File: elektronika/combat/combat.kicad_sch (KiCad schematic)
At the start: 4 parts, among them J1 Conn_01x04_Pin, U1 ESP32-S3-WROOM, U2 TB6612FNG, U3 L78M05CDT

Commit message: schemat pcb prawie gotowy
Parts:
- removed U3: L78M05CDT, VREG_L78M05CDT, symbol L78M05CDT:L78M05CDT
- added C1: 10uF, symbol Device:C
- added C2: 22uF, symbol Device:C
- added D1: D_Schottky, Diode_THT:D_DO-41_SOD81_P10.16mm_Horizontal, symbol Device:D_Schottky
- added J2: naped_prawy, TerminalBlock:TerminalBlock_MaiXu_MX126-5.0-02P_1x02_P5.00mm, symbol Connector:Screw_Terminal_01x02
- added J3: naped_lewy, TerminalBlock:TerminalBlock_MaiXu_MX126-5.0-02P_1x02_P5.00mm, symbol Connector:Screw_Terminal_01x02
- added R1: 240, PCM_SparkFun-Resistor:R_0603_1608Metric, symbol PCM_SparkFun-Resistor:R
- added R2: 390, PCM_SparkFun-Resistor:R_0603_1608Metric, symbol PCM_SparkFun-Resistor:R
- added U3: AMS1117, Package_TO_SOT_SMD:SOT-223-3_TabPin2, symbol Regulator_Linear:AMS1117
- added U4: przetwornica, Connector_PinHeader_1.00mm:Bez_nazwy, symbol chuj_wie:przetwornica_pot
- J1: footprint (none) -> Connector_PinHeader_2.54mm:PinHeader_1x04_P2.54mm_Vertical
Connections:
- net GND: now reaches U2.10 (PGND2), U2.9 (PGND2)
- net GND: now also J1.4 (Pin_4), U1.1 (GND), U1.40 (GND), U1.41.1 (GND), U1.41.2 (GND), U1.41.3 (GND), U1.41.4 (GND), U1.41.5 (GND), U1.41.6 (GND), U1.41.7 (GND), U1.41.8 (GND), U1.41.9 (GND), U2.18 (GND), U2.3 (PGND1), U2.4 (PGND1), C1.2, C2.1, R2.2, U4. (IN+)
- net +3.3V: now reaches U2.19 (STBY)
- net +3.3V: now also U1.2 (VDD), C2.2, D1.2 (A), R1.1, U3.2 (VO)
- net +5V: now reaches U2.20 (VCC)
- net +5V: now also J1.3 (Pin_3), C1.1, D1.1 (K), U3.3 (VI), U4. (IN+)
- net RX: now reaches J1.1 (Pin_1)
- net RX: now also U1.10 (IOA17)
- net TX: now reaches J1.2 (Pin_2)
- net TX: now also U1.11 (IOA18)
- new net: R1.2, R2.1, U3.1 (ADJ)
- new net 11.1V: U4. (IN+)
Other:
- moved on the sheet: J1

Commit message: płytka pcb bez footprinta
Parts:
- removed U1: ESP32-S3-WROOM, PCM_SparkFun-RF:ESP32-S3-WROOM-1, symbol PCM_SparkFun-RF:ESP32-S3-WROOM
- removed U2: TB6612FNG, Package_SO:SSOP-24_5.3x8.2mm_P0.65mm, symbol Driver_Motor:TB6612FNG
- added C5: 1u, Capacitor_SMD:C_0603_1608Metric, symbol Device:C
- added D2: RED, LED_SMD:LED_0603_1608Metric, symbol Device:LED
- added D3: GREEN, LED_SMD:LED_0603_1608Metric, symbol Device:LED
- added D4: BLUE, LED_SMD:LED_0603_1608Metric, symbol Device:LED
- added J4: TYPE-C-31-M-12, TYPE-C-31-M-12:HRO_TYPE-C-31-M-12, symbol TYPE-C-31-M-12:TYPE-C-31-M-12
- added R3, R4, R5, R6, R7, R8: 5.1K, Resistor_SMD:R_0603_1608Metric, symbol Device:R
- added SW1, SW2: TS-1088-AR02016, easyeda2kicad:SW-SMD_L3.9-W3.0-P4.45, symbol easyeda2kicad:TS-1088-AR02016
- added TB1: POLOLU-713, foots:SHIELD_POLOLU-713, symbol POLOLU-713:POLOLU-713
- added U1: ESP32-S3-WROOM-1, Espressif:ESP32-S3-WROOM-1, symbol Espressif:ESP32-S3-WROOM-1
- R1: value 240 -> 390
- R2: value 390 -> 240
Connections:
- net +3.3V: now also U1.2 (3V3)
- net +5V: now also J4.A4_B9 (VBUS), J4.B4_A9 (VBUS), R5.1
- net GND: now also C5.2, D2.1 (K), D3.1 (K), D4.1 (K), J4.A1_B12 (GND), J4.B1_A12 (GND), J4.S1 (SHIELD), J4.S2 (SHIELD), J4.S3 (SHIELD), J4.S4 (SHIELD), R3.2, R4.2, SW1.1, SW2.1, TB1.1 (GND), TB1.8 (GND), TB1.9 (GND)
- net RX: now also U1.10 (GPIO17/U1TXD/ADC2_CH6)
- net TX: now also U1.11 (GPIO18/U1RXD/ADC2_CH7/CLK_OUT3)
- net B01: now reaches J2.1 (Pin_1)
- net B01: now also TB1.6 (BO1)
- net B02: now reaches J2.2 (Pin_2)
- net B02: now also TB1.5 (BO2)
- net A01: now reaches J3.1 (Pin_1)
- net A01: now also TB1.3 (AO1)
- net A02: now reaches J3.2 (Pin_2)
- net A02: now also TB1.4 (AO2)
- new net: D4.2 (A), R7.2
- new net: D2.2 (A), R5.2
- new net: J4.B5 (CC2), R4.1
- new net: D3.2 (A), R6.2
- new net: J4.A5 (CC1), R3.1
- new net: U1.1 (GND), U1.40 (GND), U1.41 (GND)
- new net +3V3: R6.1, R8.1
- new net 3V3: TB1.13 (~{STBY})
- new net D+: J4.A6 (DP1), J4.B6 (DP2), U1.14 (GPIO20/U1CTS/ADC2_CH9/CLK_OUT1/USB_D+)
- new net D-: J4.A7 (DN1), J4.B7 (DN2), U1.13 (GPIO19/U1RTS/ADC2_CH8/CLK_OUT2/USB_D-)
- new net EN: C5.1, R8.2, SW1.2, U1.3 (EN)
- new net GPIO0: SW2.2, U1.27 (GPIO0/BOOT)
- new net GPIO21: R7.1, U1.23 (GPIO21)
- no-connect marks 0 -> 2

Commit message: gotowy schemat pcb bez footow
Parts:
- added J5: Screw_Terminal_01x03, symbol Connector:Screw_Terminal_01x03
- added U2: (no value), symbol SterownikBLDC:BLDC_BlHeli
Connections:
- net 11.1V: now also TB1.7 (VMOT), U2. (GND)
- net 3V3: now also TB1.2 (VCC)
- net GND: now also U1.1 (GND), U1.40 (GND), U1.41 (GND), U2. (GND)
- net GPIO10: now reaches TB1.10 (PWMB)
- net GPIO10: now also U1.18 (GPIO10/TOUCH10/ADC1_CH9/FSPICS0/FSPIIO4/SUBSPICS0)
- net GPIO9: now reaches TB1.11 (BIN2)
- net GPIO9: now also U1.17 (GPIO9/TOUCH9/ADC1_CH8/FSPIHD/SUBSPIHD)
- net GPIO8: now reaches TB1.12 (BIN1)
- net GPIO8: now also U1.12 (GPIO8/TOUCH8/ADC1_CH7/SUBSPICS1)
- net GPIO5: now reaches TB1.14 (AIN1)
- net GPIO5: now also U1.5 (GPIO5/TOUCH5/ADC1_CH4)
- net GPIO6: now reaches TB1.15 (AIN2)
- net GPIO6: now also U1.6 (GPIO6/TOUCH6/ADC1_CH5)
- net GPIO7: now reaches TB1.16 (PWMA)
- net GPIO7: now also U1.7 (GPIO7/TOUCH7/ADC1_CH6)
- net ePWM: now reaches U1.4 (GPIO4/TOUCH4/ADC1_CH3)
- net ePWM: now also U2. (GND)
- new net: J5.1 (Pin_1), U2. (GND)
- new net: J5.2 (Pin_2), U2. (GND)
- new net: J5.3 (Pin_3), U2. (GND)
- no-connect marks 2 -> 25
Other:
- moved on the sheet: J4, R3, R4, TB1

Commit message: nowsza wersja schematu
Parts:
- added H1, H2, H3, H4: MountingHole, symbol Mechanical:MountingHole
- C1: footprint (none) -> Capacitor_SMD:C_0805_2012Metric_Pad1.18x1.45mm_HandSolder
- C2: footprint (none) -> Capacitor_SMD:C_1210_3225Metric_Pad1.33x2.70mm_HandSolder
- J4: footprint TYPE-C-31-M-12:HRO_TYPE-C-31-M-12 -> Connector_USB:USB_C_Receptacle_HRO_TYPE-C-31-M-12
- J5: footprint (none) -> PCM_SparkFun-Connector:ScrewTerminal_1x03_P3.5mm_Blue
- SW1, SW2: footprint easyeda2kicad:SW-SMD_L3.9-W3.0-P4.45 -> foots:PTS125SM73SMTR21MLFS
- U2: value (none) -> kontroler_bldc

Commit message: gotowy footprint
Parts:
- removed J4: TYPE-C-31-M-12, Connector_USB:USB_C_Receptacle_HRO_TYPE-C-31-M-12, symbol TYPE-C-31-M-12:TYPE-C-31-M-12
- removed R3, R4: 5.1K, Resistor_SMD:R_0603_1608Metric, symbol Device:R
- removed SW1, SW2: TS-1088-AR02016, foots:PTS125SM73SMTR21MLFS, symbol easyeda2kicad:TS-1088-AR02016
- added J4: USB_C_Receptacle_USB2.0_14P, Connector_USB:USB_C_Receptacle_HRO_TYPE-C-31-M-12, symbol Connector:USB_C_Receptacle_USB2.0_14P
- added J6: Conn_02x04_Odd_Even, Connector_PinHeader_2.54mm:PinHeader_2x04_P2.54mm_Vertical, symbol Connector_Generic:Conn_02x04_Odd_Even
- added J7: Conn_01x02, PCM_SparkFun-Connector:ScrewTerminal_1x02_P3.5mm_Blue, symbol Connector_Generic:Conn_01x02
- added R10, R11: 5.1K, Resistor_SMD:R_0603_1608Metric, symbol Device:R
- added SW1, SW3: SW_DIP_x01, foots:gownoklik, symbol Switch:SW_DIP_x01
- H1, H2, H3, H4: footprint (none) -> MountingHole:MountingHole_3.2mm_M3
- J2, J3: footprint TerminalBlock:TerminalBlock_MaiXu_MX126-5.0-02P_1x02_P5.00mm -> PCM_SparkFun-Connector:ScrewTerminal_1x02_P3.5mm_Blue
- R6, R7: value 5.1K -> 1k
- U2: footprint (none) -> foots:BLDC
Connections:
- net +5V: now also U4.3 (OUT+), J4.A4 (VBUS), J4.A9 (VBUS), J4.B4 (VBUS), J4.B9 (VBUS); no longer U4. (IN+)
- net 11.1V: now also U2.1 (+11.1V), U4.4 (IN+); no longer U2. (GND), U4. (IN+)
- net 3V3: now also J6.1 (Pin_1)
- net D+: now also J4.A6 (D+), J4.B6 (D+)
- net D-: now also J4.A7 (D-), J4.B7 (D-)
- net EN: now also SW1.2
- net GND: now also U2.3 (LGND), U2.4 (GND), U4.1 (OUT-), U4.2 (IN-), J4.A1 (GND), J4.A12 (GND), J4.B1 (GND), J4.B12 (GND), J4.SH (SHIELD), J6.8 (Pin_8), R10.2, R11.2, SW1.1, SW3.1; no longer U2. (GND), U4. (IN+)
- net GPIO0: now also SW3.2
- net RX: now also J6.2 (Pin_2)
- net TX: now also J6.7 (Pin_7)
- net ePWM: now also U2.2 (PWM); no longer U2. (GND)
- net at J5.1 (Pin_1): now also U2.7 (-); no longer U2. (GND)
- net at J5.2 (Pin_2): now also U2.6 (PWM); no longer U2. (GND)
- net at J5.3 (Pin_3): now also U2.5 (+); no longer U2. (GND)
- new net: J4.A5 (CC1), R10.1
- new net: J4.B5 (CC2), R11.1
- no-connect marks 25 -> 27
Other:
- moved on the sheet: C5, J1, R8

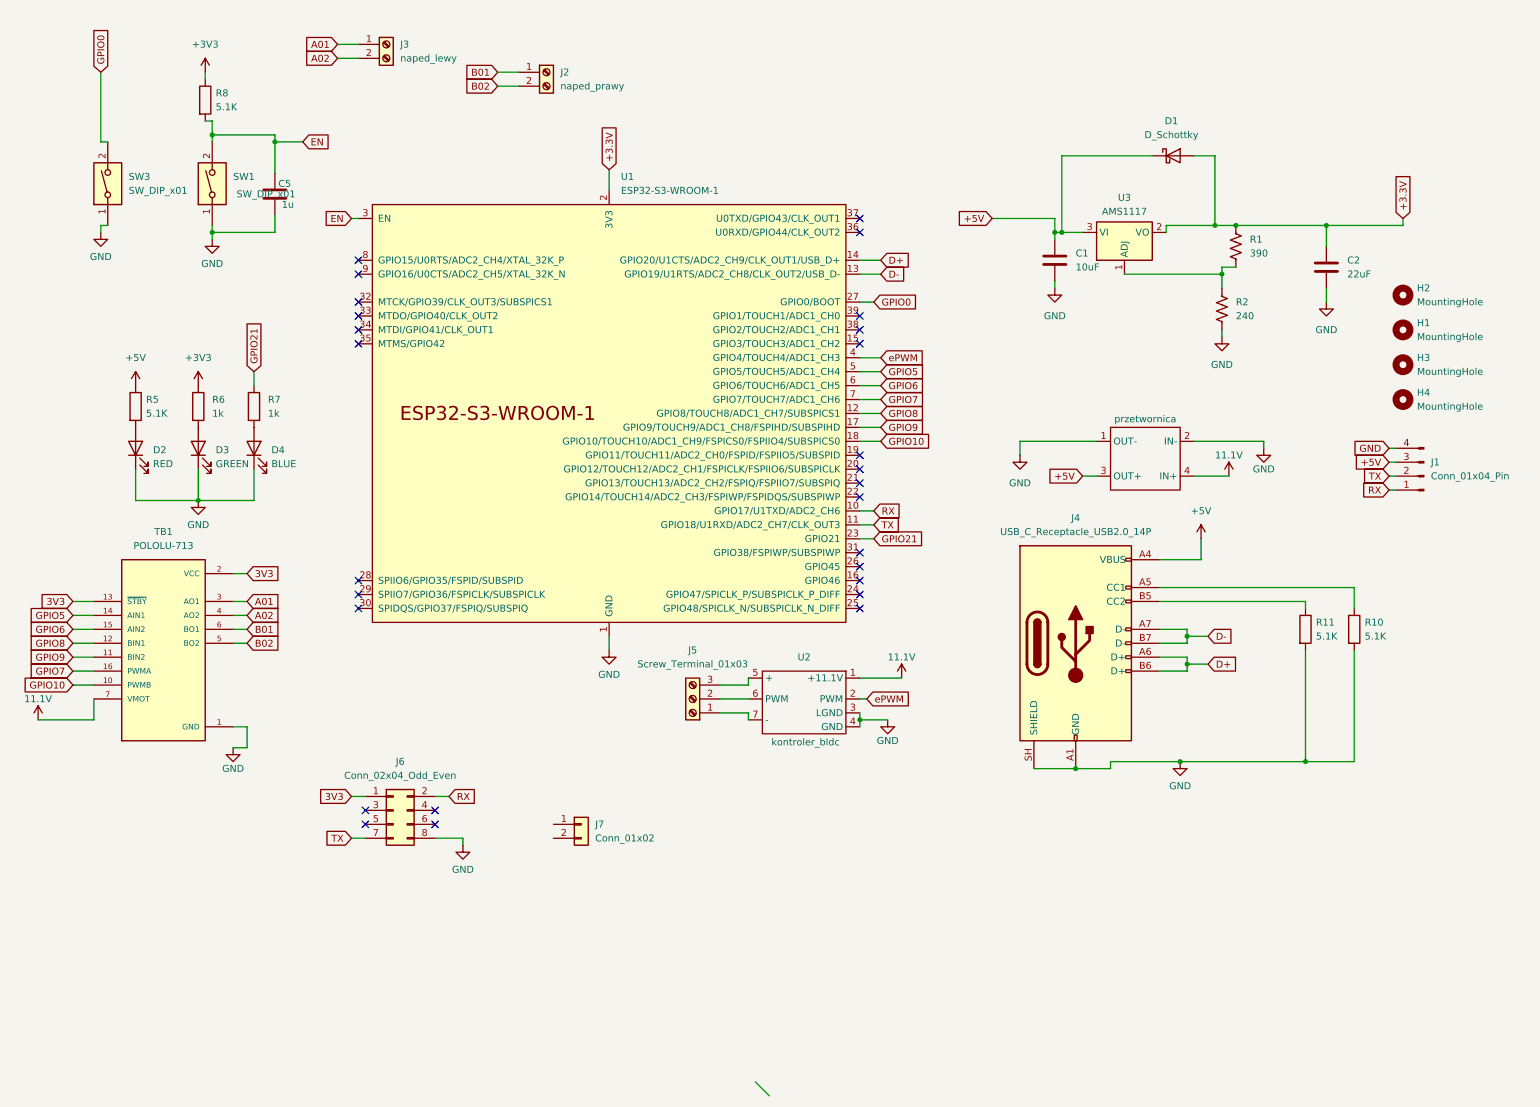
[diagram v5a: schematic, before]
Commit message: lepsza wersja pcb, layout jeszcze do zrobienia
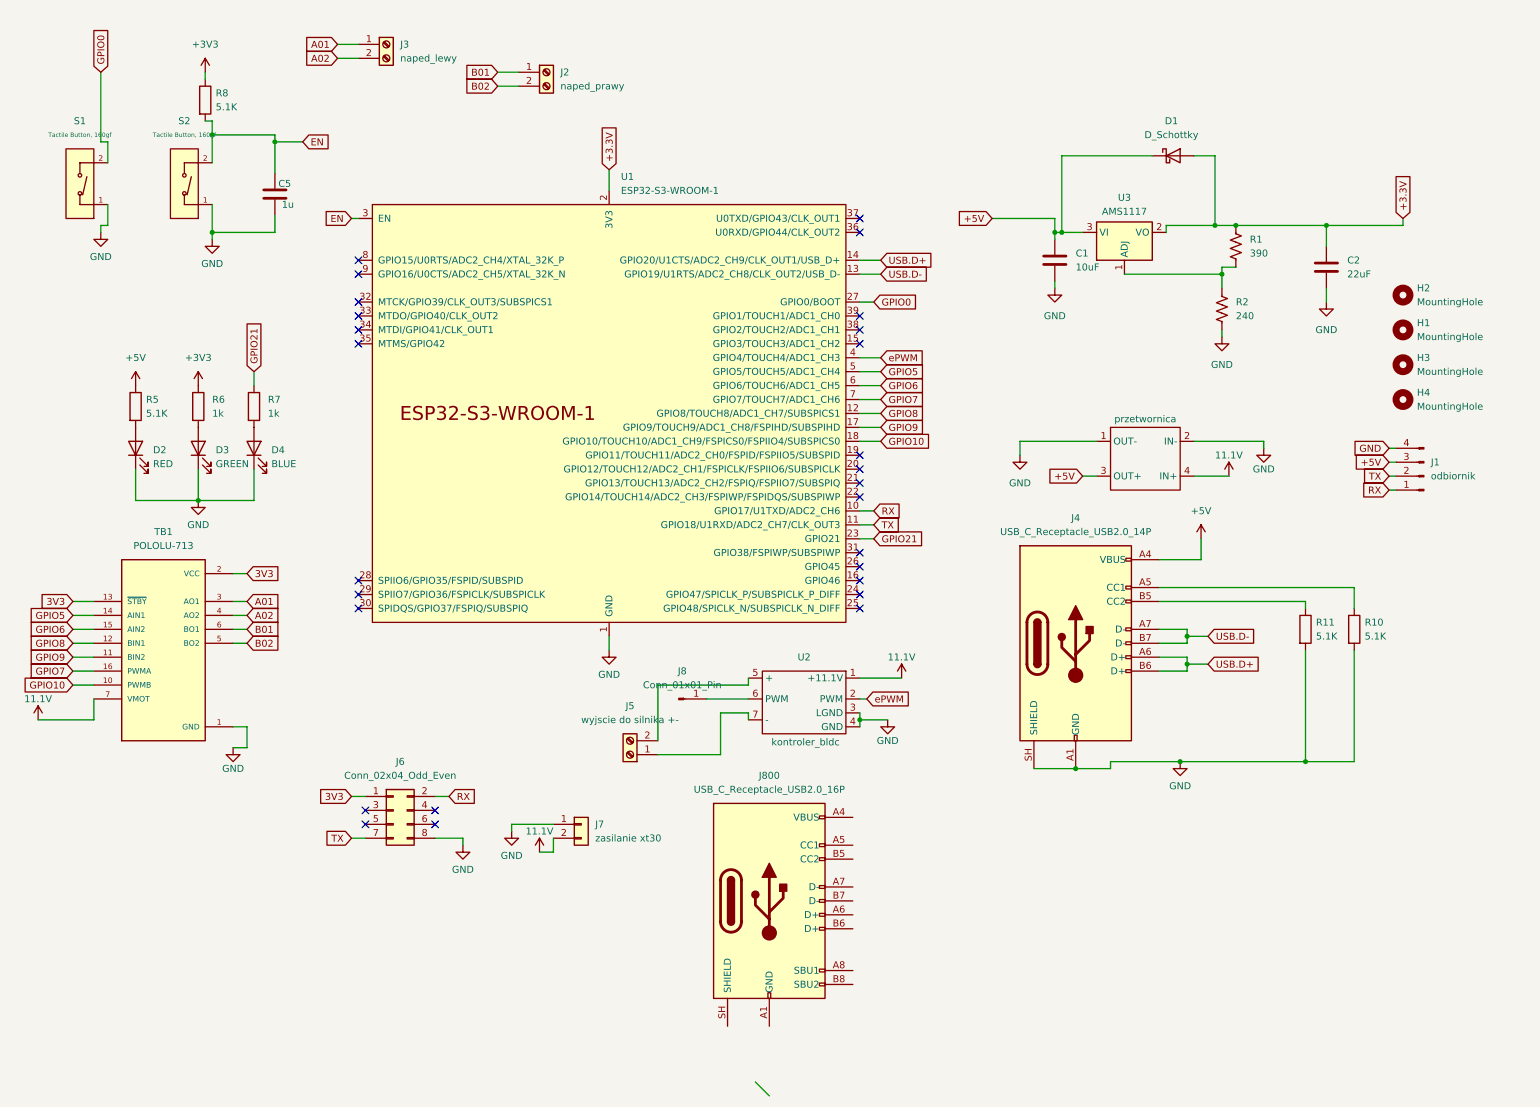
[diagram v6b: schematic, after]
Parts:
- removed J5: Screw_Terminal_01x03, PCM_SparkFun-Connector:ScrewTerminal_1x03_P3.5mm_Blue, symbol Connector:Screw_Terminal_01x03
- removed SW1, SW3: SW_DIP_x01, foots:gownoklik, symbol Switch:SW_DIP_x01
- added J5: wyjscie do silnika +-, Connector_AMASS:AMASS_XT30PW-F_1x02_P2.50mm_Horizontal, symbol Connector:Screw_Terminal_01x02
- added J8: Conn_01x01_Pin, Connector_Wire:SolderWire-0.1sqmm_1x01_D0.4mm_OD1mm, symbol Connector:Conn_01x01_Pin
- added J800: USB_C_Receptacle_USB2.0_16P, Connector_USB:USB_C_Receptacle_GCT_USB4105-xx-A_16P_TopMnt_Horizontal, symbol Connector:USB_C_Receptacle_USB2.0_16P
- added S1, S2: Tactile Button, 160gf, PCM_JLCPCB:SW_TS-1088-AR02016, symbol PCM_JLCPCB-Connectors_Buttons:Tactile Button, 160gf, 12V, 50mA, 4.0mm
- J1: value Conn_01x04_Pin -> odbiornik
- J2, J3: footprint PCM_SparkFun-Connector:ScrewTerminal_1x02_P3.5mm_Blue -> Connector_AMASS:AMASS_XT30PW-F_1x02_P2.50mm_Horizontal
- J7: value Conn_01x02 -> zasilanie xt30; footprint PCM_SparkFun-Connector:ScrewTerminal_1x02_P3.5mm_Blue -> Connector_AMASS:AMASS_XT30PW-F_1x02_P2.50mm_Horizontal
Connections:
- net 11.1V: now also J7.2 (Pin_2)
- net EN: now also S2.2 (B)
- net GND: now also J7.1 (Pin_1), S1.1 (A), S2.1 (A)
- net GPIO0: now also S1.2 (B)
- net at U2.7 (-): now also J5.1 (Pin_1)
- net at U2.6 (PWM): now also J8.1 (Pin_1)
- net at U2.5 (+): now also J5.2 (Pin_2)
- net D+ renamed USB.D+
- net D- renamed USB.D-
- new net: J800.A1 (GND), J800.A12 (GND), J800.B1 (GND), J800.B12 (GND)
- new net: J800.A4 (VBUS), J800.A9 (VBUS), J800.B4 (VBUS), J800.B9 (VBUS)

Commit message: pcb v1.0
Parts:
- removed J4: USB_C_Receptacle_USB2.0_14P, Connector_USB:USB_C_Receptacle_HRO_TYPE-C-31-M-12, symbol Connector:USB_C_Receptacle_USB2.0_14P
- added J4: buzzer, Connector_PinSocket_2.54mm:PinSocket_1x02_P2.54mm_Vertical, symbol Connector_Generic:Conn_01x02
- J2, J3, J5, J7: footprint Connector_AMASS:AMASS_XT30PW-F_1x02_P2.50mm_Horizontal -> Connector_AMASS:AMASS_XT30U-F_1x02_P5.0mm_Vertical
- J8: footprint Connector_Wire:SolderWire-0.1sqmm_1x01_D0.4mm_OD1mm -> Connector_PinHeader_2.54mm:PinHeader_1x01_P2.54mm_Vertical
- TB1: MANUFACTURER POLOLU -> (none); Manufacturer (none) -> POLOLU
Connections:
- net +5V: now also J800.A4 (VBUS), J800.A9 (VBUS), J800.B4 (VBUS), J800.B9 (VBUS)
- net GND: now also J800.A1 (GND), J800.A12 (GND), J800.B1 (GND), J800.B12 (GND), J800.SH (SHIELD), J4.2 (Pin_2)
- net USB.D+: now also J800.A6 (D+), J800.B6 (D+)
- net USB.D-: now also J800.A7 (D-), J800.B7 (D-)
- net at J800.A5 (CC1): now also R10.1
- net at J800.B5 (CC2): now also R11.1
- net john: now reaches U1.32 (MTCK/GPIO39/CLK_OUT3/SUBSPICS1)
- net john: now also J4.1 (Pin_1)
- no-connect marks 27 -> 28
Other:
- moved on the sheet: J800

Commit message: PCB v1.2
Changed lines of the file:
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@@
 	(generator_version "10.0")
 	(paper "A4")
+	(rectangle
+		(start 179.07 43.18)
+		(end 274.32 92.71)
+		(stroke
+			(width 0)
+			(type default)
+		)
+		(fill
+			(type none)
+		)
+	)
 	(junction
 		(at 46.99 66.04)
